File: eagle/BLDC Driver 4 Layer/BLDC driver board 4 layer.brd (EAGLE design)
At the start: 40 parts, among them Q1 CSD173XXQX-NEXFET, Q2 CSD173XXQX-NEXFET, Q3 CSD173XXQX-NEXFET, Q4 CSD173XXQX-NEXFET, Q5 CSD173XXQX-NEXFET, Q6 CSD173XXQX-NEXFET

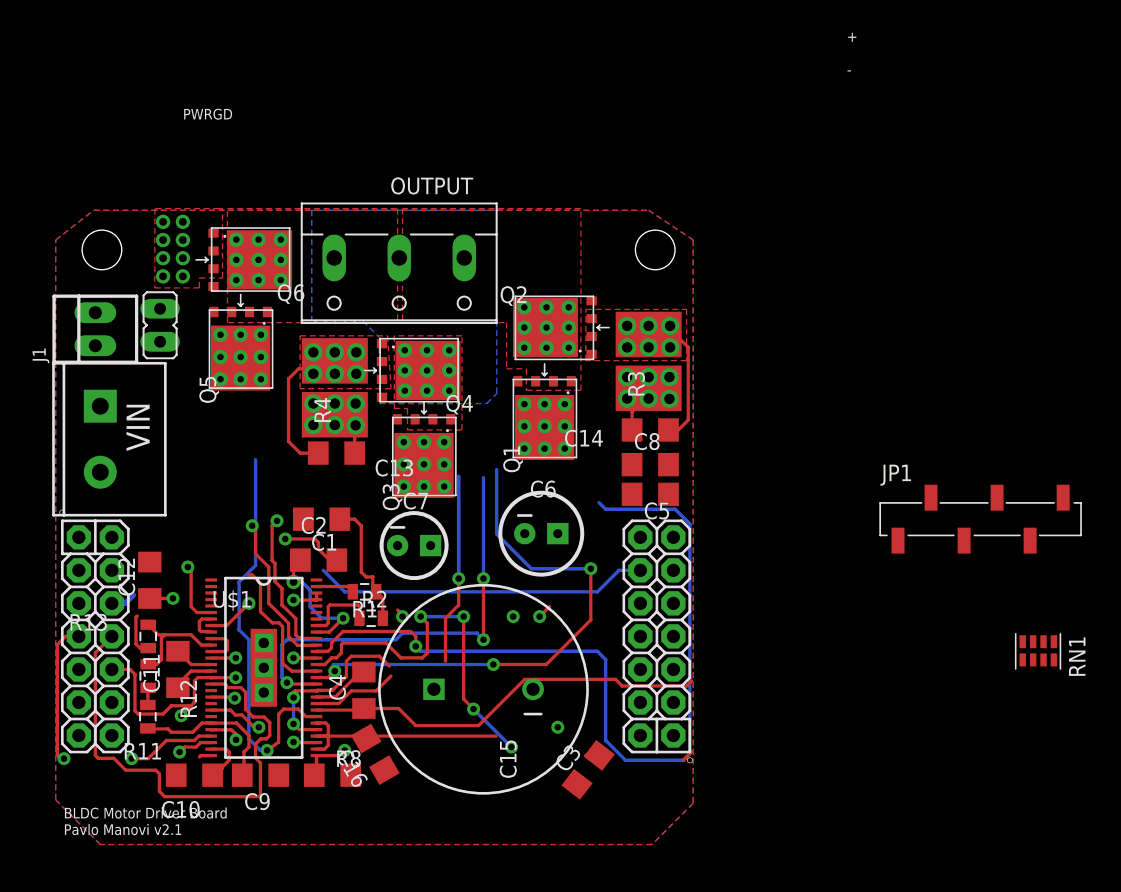
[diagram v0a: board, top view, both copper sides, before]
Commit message: More BLDC work.  Updated ASL.lbr.
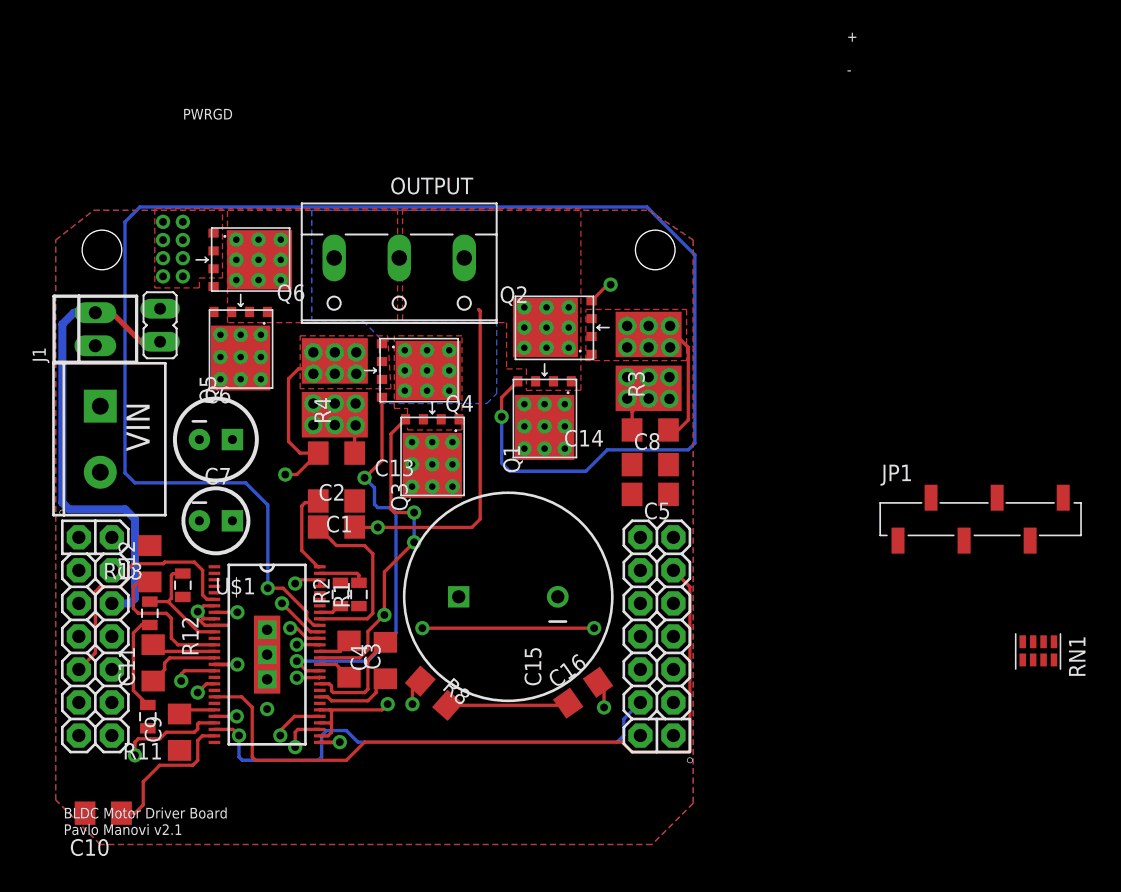
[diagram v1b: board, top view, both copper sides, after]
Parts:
- moved C6 26.0 mm to (15.0, 31.8)
- moved C3 20.3 mm to (25.2, 14.8), turned to 270 degrees
- moved C16 16.7 mm to (43.2, 12.2), turned to 35 degrees
- moved C7 15.4 mm to (15.0, 25.4)
- moved R8 10.0 mm to (31.8, 12.1), turned to 138.5 degrees
- moved C10 7.59 mm to (6.32, 2.92)
- moved C15 7.36 mm to (37.5, 19.6)
- moved C9 7.04 mm to (12.2, 9.14), turned to 270 degrees
- moved R12 4.83 mm to (9.91, 18.3)
- moved R13 4.76 mm to (12.4, 20.4)
- moved R2 2.99 mm to (24.6, 19.7), turned to 90 degrees
- moved C2 2.89 mm to (24.3, 24.9)
- moved C4 2.82 mm to (28.0, 14.7)
- moved C11 1.97 mm to (10.2, 14.5)
- moved C1 1.81 mm to (24.3, 26.9)
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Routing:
- net GH_A: track 15.5 -> 126.4 mm, vias 1 -> 2
- net 3V3: track 78.6 -> 23.1 mm, vias 4 -> 3
- net VCC: track 1.91 -> 36.7 mm
- net GL_C: track 30.6 -> 0.00 mm, vias 1 -> 0
- net PWM1: track 37.5 -> 9.95 mm, vias 0 -> 1
- net OUTPUTC: track 32.2 -> 6.08 mm
- net QEI-INDEX: track 25.8 -> 0.00 mm
- net N$6: track 28.1 -> 2.66 mm, vias 4 -> 0
- net QEI-B: track 24.9 -> 0.00 mm
- net GH_B: track 49.7 -> 25.2 mm, vias 2 -> 3
- net OUTPUTA: track 20.0 -> 41.6 mm
- net GH_C: track 21.2 -> 0.00 mm, vias 1 -> 0
- net SN1: track 28.9 -> 49.9 mm, vias 2 -> 3
- net OUTPUTB: track 21.7 -> 2.67 mm, vias 2 -> 0
- net SN2: track 41.5 -> 25.4 mm, vias 3 -> 2
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
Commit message: Completed BLDC 4-layer and new Ether-shield
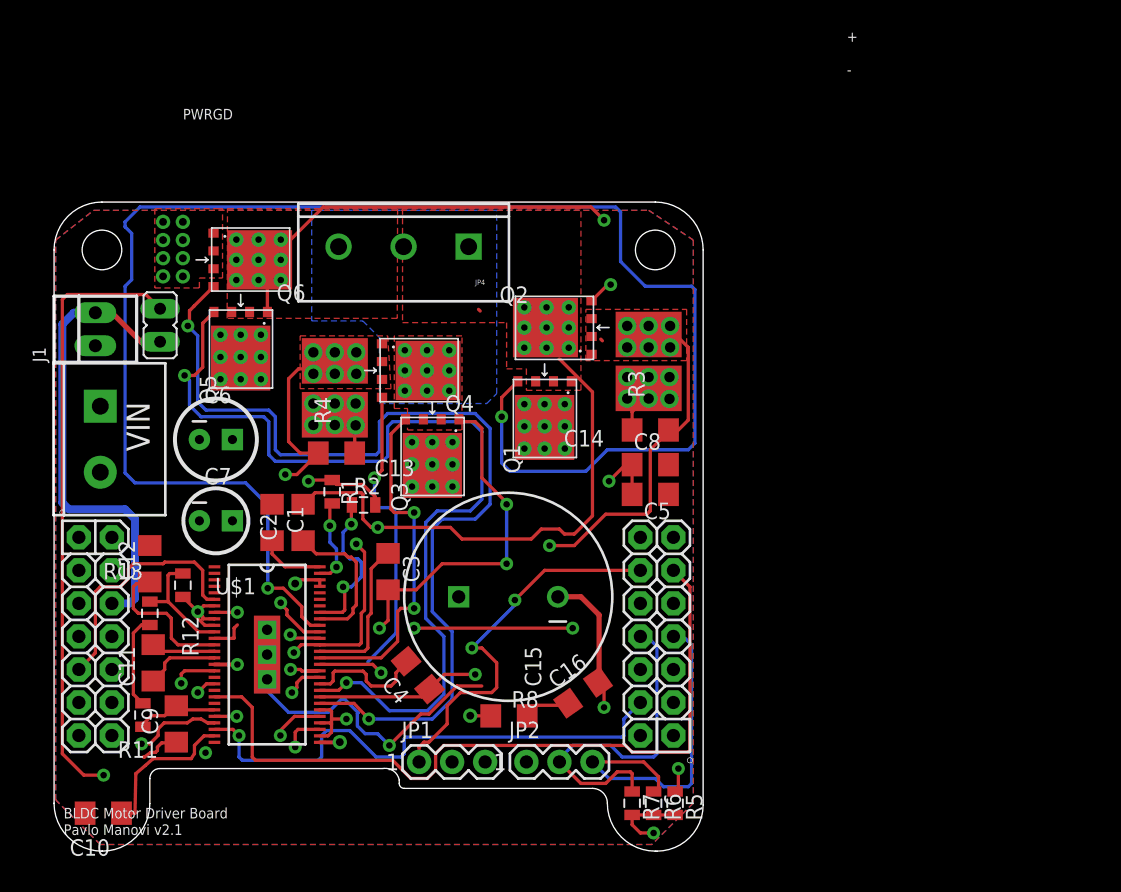
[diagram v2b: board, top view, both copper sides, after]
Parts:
- removed OUTPUT: (no value), con-wago-500:W237-103
- removed RN1: (no value), ASL:EXB-38V271JV
- added JP2: M03PTH, ASL:1X03
- added JP4: M03-SCREW-5MM, ASL:SCREWTERMINAL-5MM-3
- added R5, R6, R7: (no value), ASL:0805
- JP1: value (none) -> M03PTH; device ASL:1X06_SMD_STRAIGHT -> ASL:1X03
- U$2: value CAN_NODE_SHIELD_V3 -> CANODE_SHIELD
- moved JP1 50.6 mm to (33.1, 6.86)
- moved R1 8.16 mm to (23.9, 27.6), turned to 90 degrees
- moved C3 7.37 mm to (28.2, 21.5)
- moved R2 7.11 mm to (26.3, 26.6), turned to 0 degrees
- moved R8 6.03 mm to (37.5, 10.4), turned to 180 degrees
- moved C1 5.22 mm to (19.3, 25.3), turned to 270 degrees
- moved C4 2.74 mm to (30.5, 13.5), turned to 310 degrees
- moved C2 2.59 mm to (21.7, 25.3), turned to 90 degrees
- moved C9 0.68 mm to (11.9, 9.78)
- moved R11 0.40 mm to (9.37, 10.5)
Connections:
- net ADC/HALL1: now also JP2.3, R6.1; no longer JP1.6, RN1.P$2
- net ADC/HALL2: now also JP2.2, R7.1; no longer JP1.5, RN1.P$3
- net ADC/HALL3: now also JP2.1, R5.1; no longer JP1.4, RN1.P$1
- net N$13: now also R5.2, R6.2, R7.2; no longer RN1.P$6, RN1.P$7, RN1.P$8
- net OUTPUTA: now also JP4.1; no longer OUTPUT.1
- net OUTPUTB: now also JP4.2; no longer OUTPUT.2
- net OUTPUTC: now also JP4.3; no longer OUTPUT.3
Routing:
- net N$13: track 0.00 -> 99.5 mm, vias 0 -> 2
- net OUTPUTC: track 6.08 -> 101.5 mm, vias 0 -> 2
- net GL_C: track 0.00 -> 74.9 mm, vias 0 -> 2
- net GH_C: track 0.00 -> 72.6 mm, vias 0 -> 2
- net QEI-A: track 0.00 -> 45.7 mm
- net SN2: track 25.4 -> 69.6 mm, vias 2 -> 4
- net QEI-B: track 0.00 -> 37.4 mm
- net GND: track 5.19 -> 41.5 mm, vias 2 -> 4
- net OUTPUTB: track 2.67 -> 34.9 mm, vias 0 -> 4
- net QEI-INDEX: track 0.00 -> 29.8 mm, vias 0 -> 2
- net ADC/HALL3: track 0.00 -> 28.4 mm, vias 0 -> 1
- net ADC/HALL1: track 0.00 -> 28.0 mm
- net ADC/HALL2: track 0.00 -> 26.4 mm
- net V_BATT: track 6.07 -> 24.5 mm, vias 3 -> 4
- net OUTPUTA: track 41.6 -> 56.1 mm
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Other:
- board outline added: 49.9 x 49.9 mm

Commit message: Polishing up 4-layer BLDC
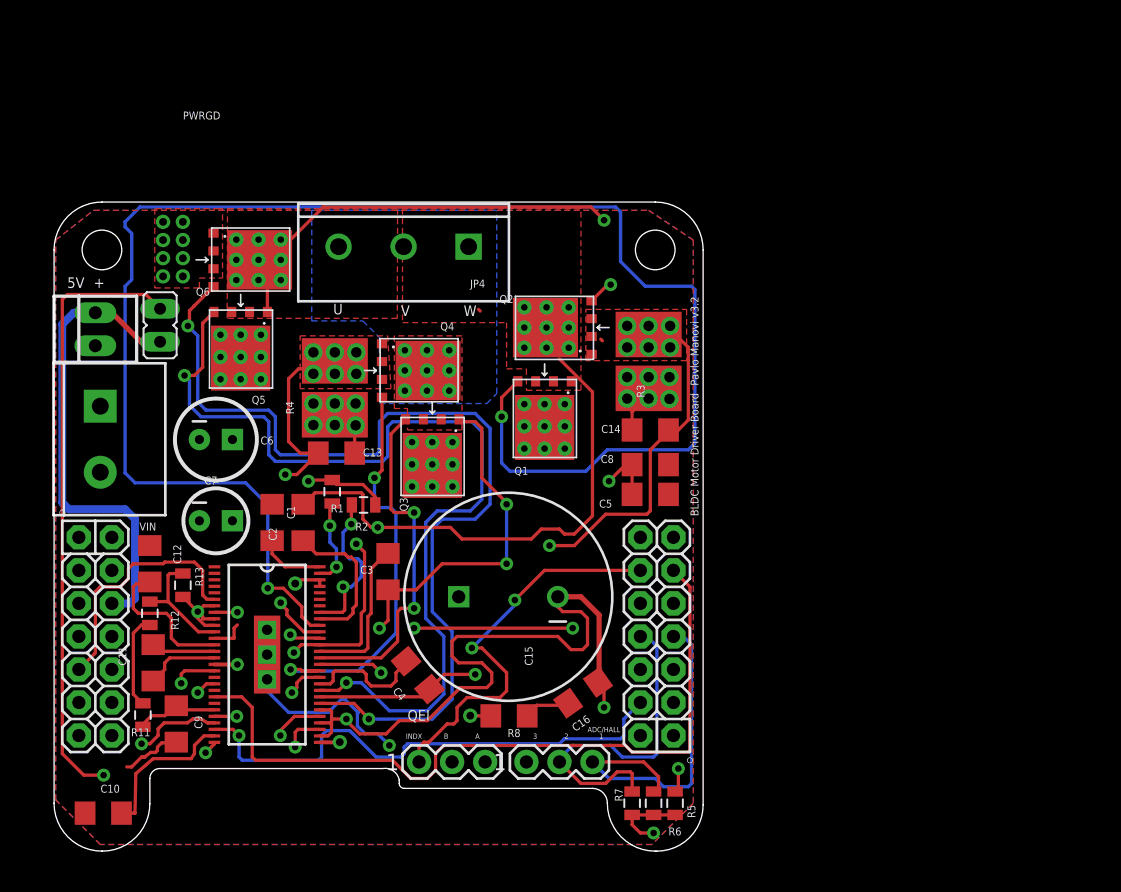
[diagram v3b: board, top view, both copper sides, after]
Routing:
- net VNEG: track 24.7 -> 60.2 mm
- net GL_B: track 25.9 -> 32.2 mm
- net GND: track 41.5 -> 35.2 mm
- net QEI-INDEX: track 29.8 -> 30.8 mm
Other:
- board text added: "1"
- board text added: "2"
- board text added: "3"
- board text added: "5V"
- board text added: "A"
- board text added: "ADC/HALL"
- board text added: "B"
- board text added: "INDX"
- board text added: "Pavlo Manovi v3.2"
- board text added: "QEI"
- board text added: "U"
- board text added: "V"
- board text added: "W"
- board text removed: "-"
- board text removed: "Pavlo Manovi v2.1"

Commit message: Ready for Board Run.
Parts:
- added R9: 3.3k, ASL:0805
- moved C10 1.66 mm to (6.12, 4.57), turned to 0 degrees
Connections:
- net 3V3: now also R9.1
- net N$2: now also R9.2
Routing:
- net 3V3: track 23.1 -> 41.3 mm, vias 3 -> 4
- net N$2: track 19.3 -> 34.0 mm, vias 0 -> 1
- net GH_A: track 127.5 -> 113.8 mm
- net N$16: track 11.7 -> 15.6 mm
- net GND: track 35.2 -> 38.3 mm, vias 4 -> 8
- net N$13: track 99.5 -> 98.7 mm
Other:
- board text removed: "PWRGD"

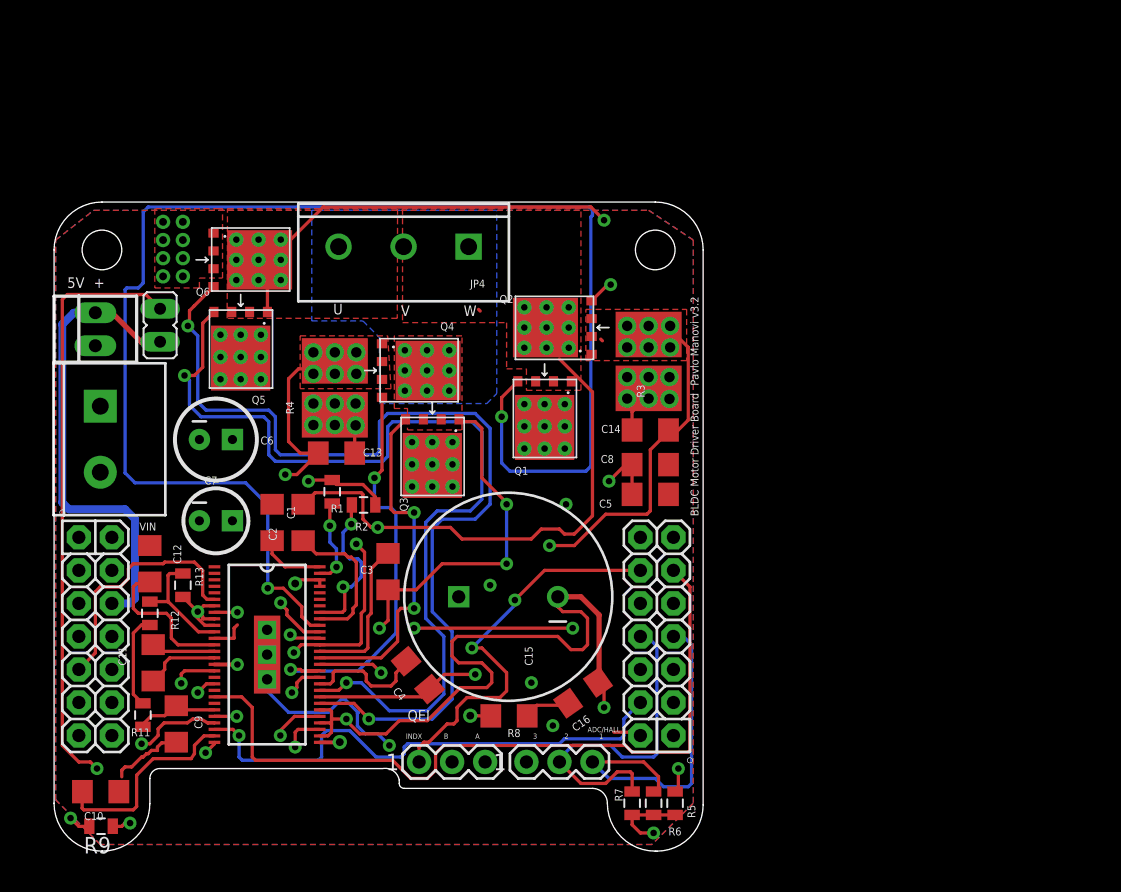
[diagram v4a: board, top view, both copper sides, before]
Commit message: Sent out boards to itead, last minute changes included.
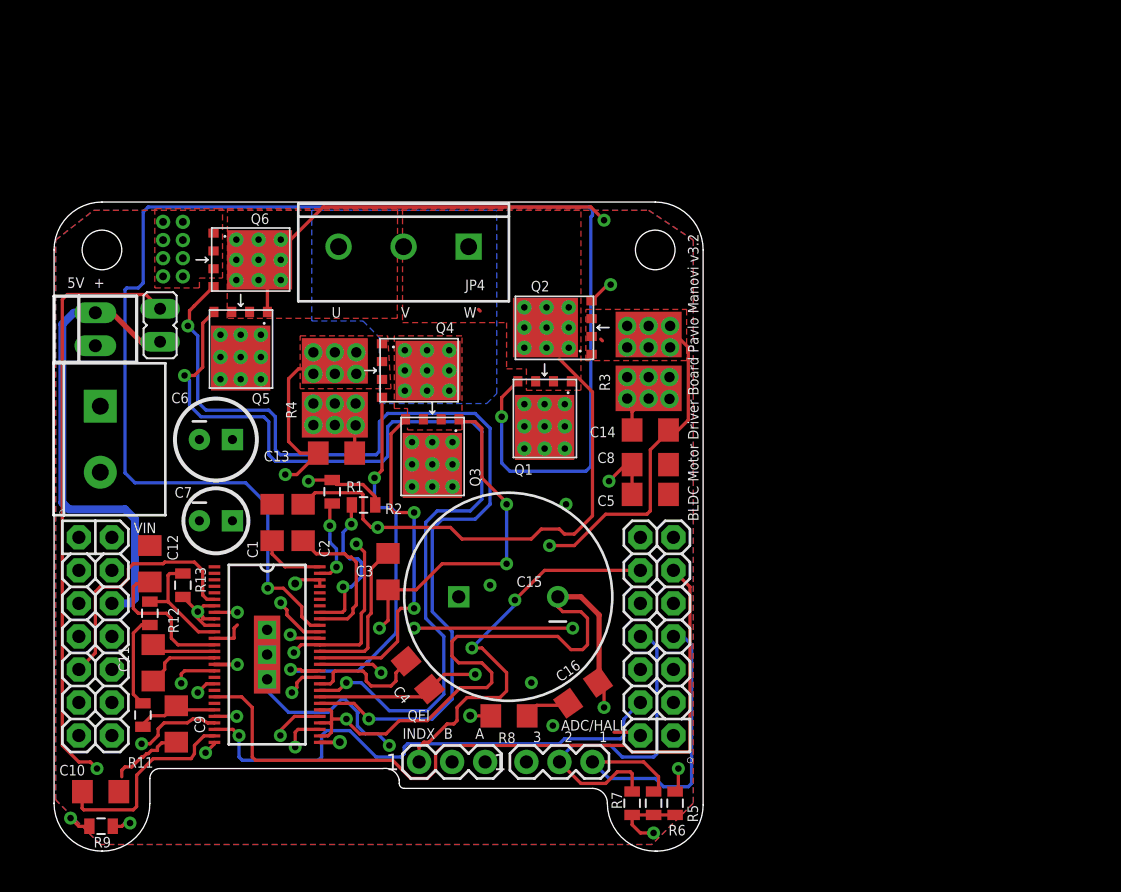
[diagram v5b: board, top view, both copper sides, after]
